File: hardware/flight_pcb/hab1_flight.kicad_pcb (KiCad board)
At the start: 4 copper layers, 95.9 x 90.2 mm, 74 parts, among them J1 BATTERY 4xL91, J10 OLED SSD1306 (bench), J11 BUZZER (+ / -), J12 EXPANSION, J2 POWER SWITCH (on the box), J3 STDC14 SWD+VCP, J4 SPI FLASH module, J5 IMU GY-601N1, J6 BAROMETER BMP390, J7 GPS MAX-M10S, J8 DS18B20 probe, J9 LoRa E22-400M22S (adapter), Q1 AO3401A, Q2 AO3400A, SW1 RESET, U1 STM32G474RET6, U2 LDL1117S33R

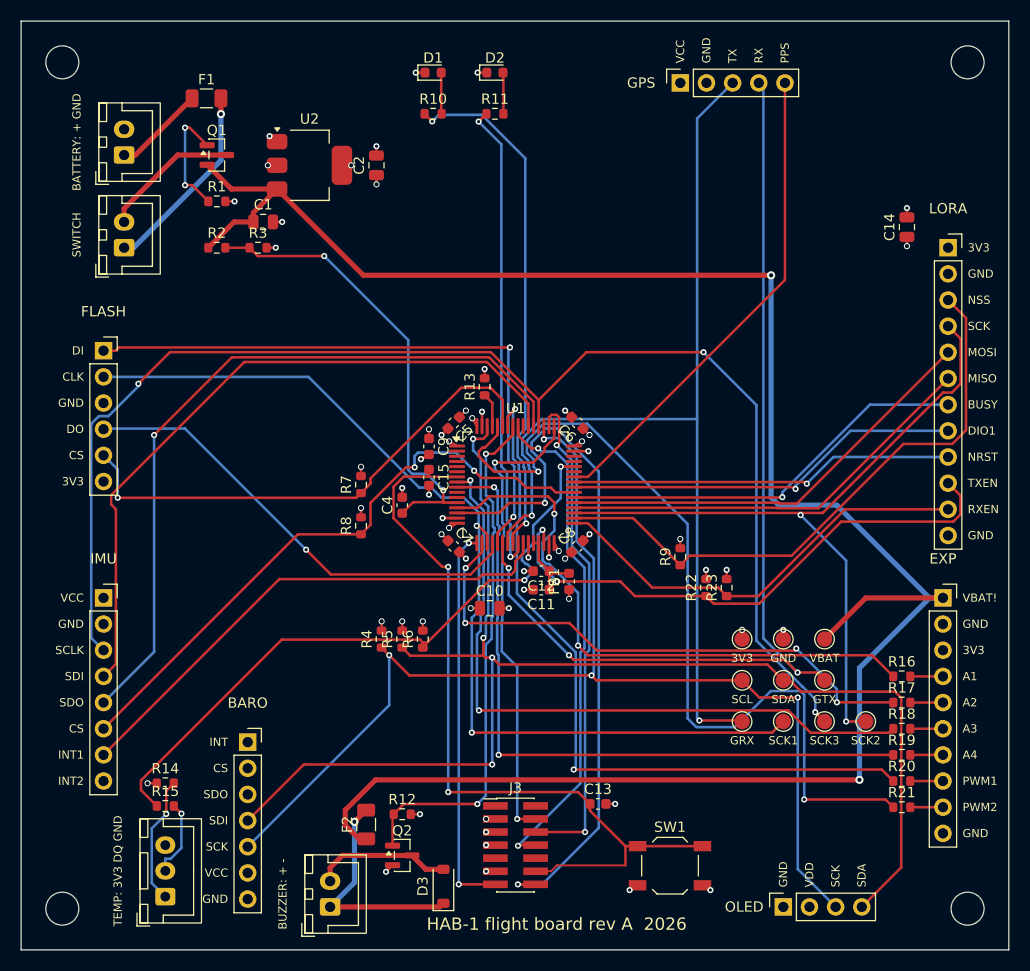
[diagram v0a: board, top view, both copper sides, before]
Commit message: flight PCB: sockets placed for the measured module boards, automatic module fit check, 1:1 print for a paper check (HW-153)
Module sizes measured from photos (pin pitch as the ruler). Flash socket turned so its
board stays on the PCB, barometer and GPS moved to the top. ERC 0/0, netlist 0
mismatches, DRC 0 unconnected, 0 parity issues.

Co-Authored-By: Claude Opus 5.5 (1M context) <noreply@anthropic.com>
Claude-Session: https://claude.ai/code/session_01Y9WTd2yaDzj6r4py6E8uJo
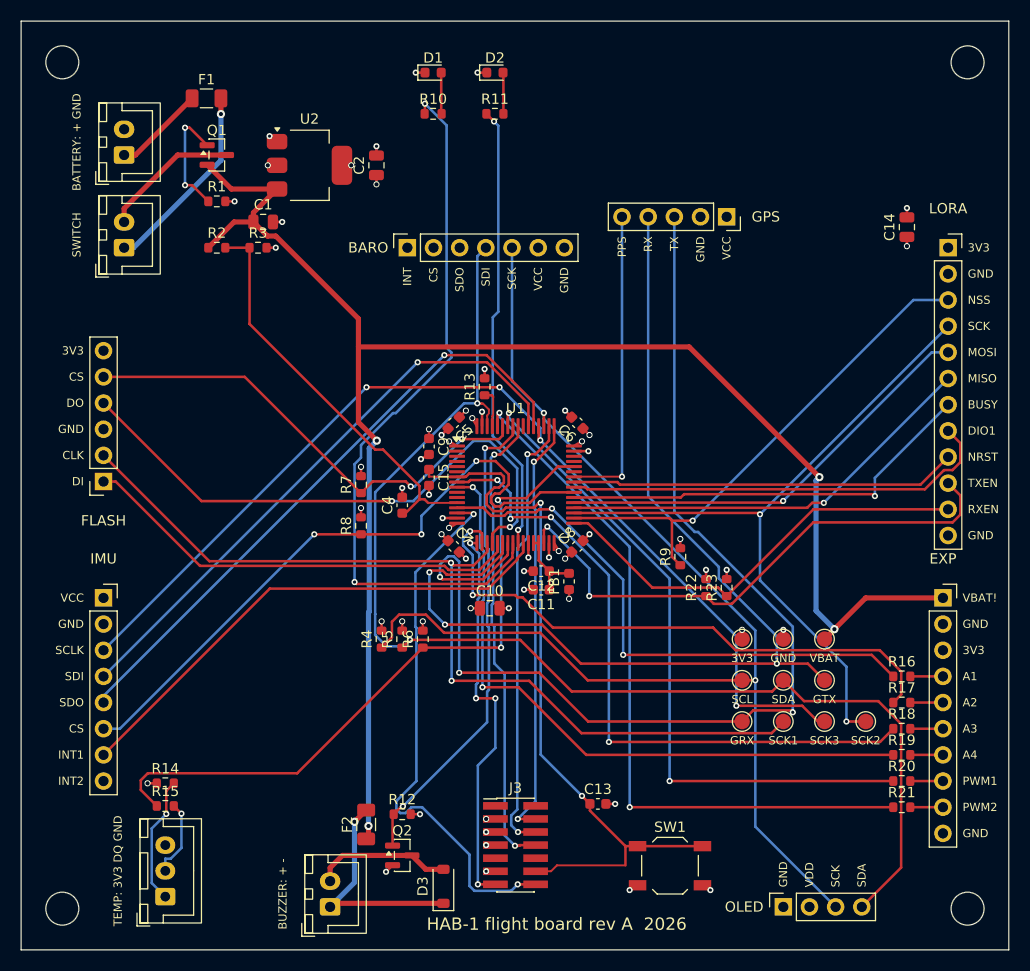
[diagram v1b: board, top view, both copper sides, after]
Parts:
- moved J6 50.4 mm to (137.5, 122.0), turned to 90 degrees
- moved J7 13.8 mm to (168.5, 119.0), turned to -90 degrees
- moved J4 12.7 mm to (108.0, 144.7), turned to 180 degrees
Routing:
- net /VBAT_PROT: track 199.9 -> 161.9 mm, vias 2 -> 4
- net /SPI3_SCK: track 132.1 -> 100.1 mm, vias 3 -> 4
- net /LED_ALIVE: track 50.8 -> 70.5 mm
- net /VCP_TX: track 70.7 -> 52.8 mm
- net /GPS_PPS: track 47.5 -> 29.9 mm, vias 0 -> 1
- net /SPI1_MOSI: track 59.6 -> 43.4 mm, vias 2 -> 0
- net /EXP_PWM2: track 85.3 -> 70.5 mm
- net /USART1_RX: track 97.3 -> 111.1 mm, vias 2 -> 3
- net /SPI3_MISO: track 72.1 -> 60.3 mm
- net /SPI1_MISO: track 45.4 -> 56.6 mm, vias 1 -> 2
- net /I2C_SDA: track 133.0 -> 122.3 mm, vias 4 -> 2
- net /SPI3_MOSI: track 68.0 -> 57.7 mm, vias 0 -> 1
- net /LORA_NSS: track 58.7 -> 50.0 mm, vias 0 -> 1
- net /SPI1_SCK: track 96.6 -> 89.3 mm
- net /EXP_PWM1: track 71.4 -> 65.2 mm
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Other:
- board text added: "BARO BMP390 board (measured, side unknown)"
- board text added: "FLASH board (measured)"
- board text added: "GPS MAX-M10S board (measured)"
- board text added: "IMU GY-601N1 board (measured)"
- board text added: "LoRa E22 adapter board (GUESS)"
- board text removed: "BARO BMP390 (module body, approx.)"
- board text removed: "FLASH (module body, approx.)"
- board text removed: "GPS MAX-M10S (module body, approx.)"
- board text removed: "IMU GY-601N1 (module body, approx.)"
- board text removed: "LoRa E22 adapter (module body, approx.)"

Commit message: flight PCB: JLCPCB files (gerbers, BOM with LCSC numbers, CPL), parts checked in the JLCPCB catalogue (HW-155)
LEDs red/yellow instead of green/blue (out of stock and too dim from 3.3 V), battery
fuse in the 24 V version, keyed programming header, via copper ring 0.15 mm.
ERC 0/0, netlist 0 mismatches, DRC 0 unconnected, 0 parity issues.

Co-Authored-By: Claude Opus 5.5 (1M context) <noreply@anthropic.com>
Claude-Session: https://claude.ai/code/session_01Y9WTd2yaDzj6r4py6E8uJo
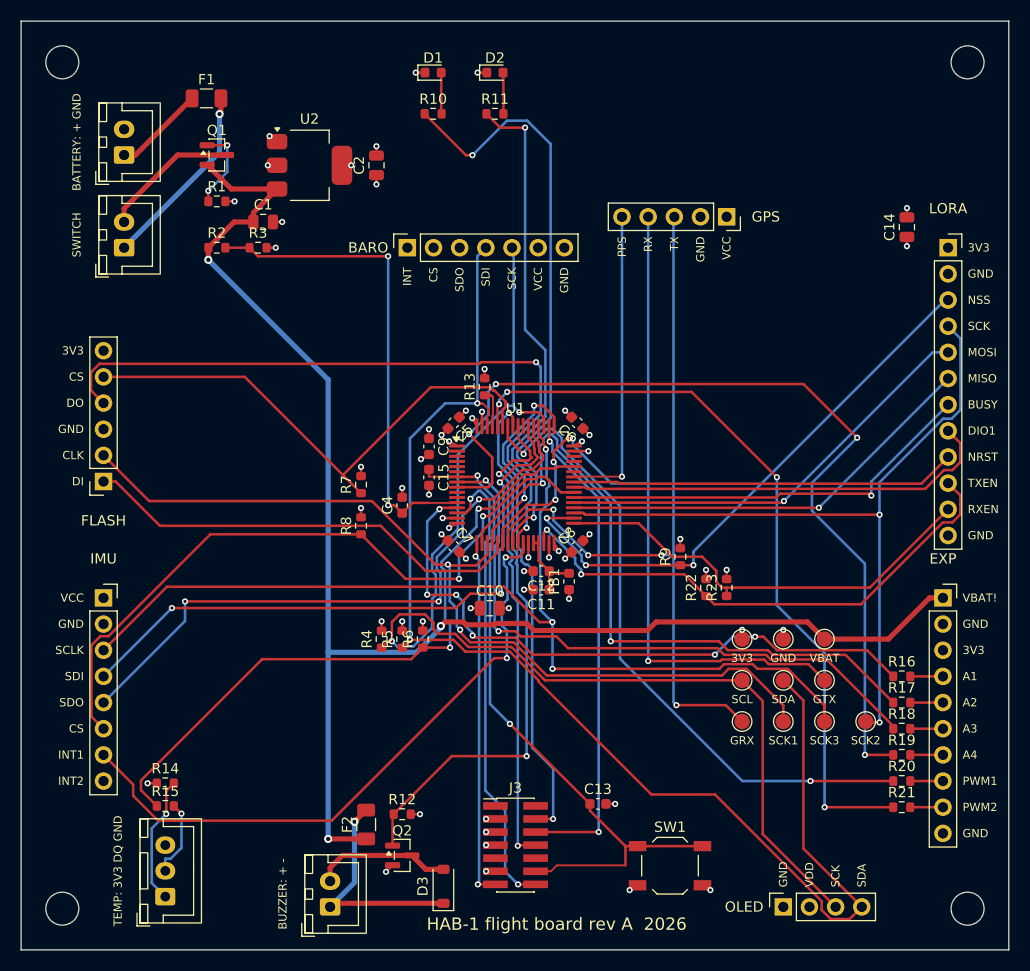
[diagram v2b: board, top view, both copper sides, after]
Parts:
- D1: value ALIVE green -> ALIVE red
- D2: value GPS FIX blue -> GPS FIX yellow
- F1: value PTC 0.5A hold -> PTC 0.5A 24V
- F2: value PTC 0.2A hold -> PTC 0.2A 24V
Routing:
- net /USART1_RX: track 111.1 -> 75.2 mm, vias 3 -> 4
- net /EXP_A4: track 64.1 -> 89.9 mm, vias 2 -> 4
- net /USART1_TX: track 102.6 -> 85.5 mm, vias 3 -> 4
- net /VBAT_PROT: track 161.9 -> 147.4 mm, vias 4 -> 3
- net /IMU_INT1: track 49.9 -> 62.2 mm, vias 0 -> 2
- net /LED_ALIVE: track 70.5 -> 58.5 mm
- net /SPI1_MISO: track 56.6 -> 68.1 mm
- net /EXP_A2: track 57.0 -> 67.0 mm
- net /EXP_A1: track 54.0 -> 61.9 mm, vias 2 -> 6
- net /BUZZER: track 46.9 -> 54.7 mm
- net /VBAT_SENSE: track 40.1 -> 47.8 mm, vias 0 -> 2
- net /VCP_TX: track 52.8 -> 45.5 mm
- net /SWDIO: track 41.5 -> 48.6 mm
- net /NRST: track 72.8 -> 66.1 mm
- net /I2C_SDA: track 122.3 -> 128.4 mm
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
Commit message: flight PCB: LoRa module E22-400M22S soldered on by JLCPCB instead of an adapter socket (HW-162, HW-155)
Own footprint from the Ebyte drawing, checked against the labels on the real module;
no tracks or vias under the module; JLCPCB part C411291 in the BOM.
ERC 0/0, netlist 0 mismatches, DRC 0 unconnected, 0 parity issues.

Co-Authored-By: Claude Opus 5.5 (1M context) <noreply@anthropic.com>
Claude-Session: https://claude.ai/code/session_01Y9WTd2yaDzj6r4py6E8uJo
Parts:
- removed J9: LoRa E22-400M22S (adapter), Connector_PinSocket_2.54mm:PinSocket_1x12_P2.54mm_Vertical
- added C16: 100n, Capacitor_SMD:C_0603_1608Metric, F.Cu at (173.5, 135.0)
- added U3: E22-400M22S, hab1:E22-400M22S, F.Cu at (184.0, 133.0)
- moved C14 22.3 mm to (173.5, 138.5)
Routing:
- net /IMU_CS: track 68.6 -> 97.3 mm, vias 2 -> 4
- net /SPI1_MISO: track 68.1 -> 46.0 mm
- net /USART1_RX: track 75.2 -> 93.9 mm, vias 4 -> 3
- net /EXP_A4: track 89.9 -> 72.2 mm, vias 4 -> 2
- net /I2C_SDA: track 128.4 -> 111.4 mm, vias 2 -> 3
- net /LED_FIX: track 48.2 -> 62.7 mm
- net /LORA_NRST: track 37.5 -> 49.2 mm, vias 0 -> 2
- net GND: track 34.0 -> 43.9 mm, vias 35 -> 46
- net /SPI2_MOSI: track 42.4 -> 51.7 mm, vias 1 -> 0
- net /SPI2_SCK: track 73.8 -> 82.9 mm, vias 2 -> 3
- net /SPI2_MISO: track 41.5 -> 50.5 mm, vias 1 -> 4
- net /EXP_A2: track 67.0 -> 60.2 mm
- net /EXP_A1: track 61.9 -> 55.6 mm, vias 6 -> 4
- net /EXP_A3: track 60.7 -> 67.0 mm
- net /EXP_PWM1: track 63.8 -> 69.9 mm, vias 2 -> 4
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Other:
- board text removed: "BUSY"
- board text removed: "DIO1"
- board text removed: "LORA"
- board text removed: "LoRa E22 adapter board (GUESS)"
- board text removed: "MISO"
- board text removed: "MOSI"
- board text removed: "NRST"
- board text removed: "NSS"
- board text removed: "RXEN"
- board text removed: "TXEN"
